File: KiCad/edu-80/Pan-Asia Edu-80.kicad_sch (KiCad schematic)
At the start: 24 parts, among them Q1 ED1402, Q2 ED1402, U1 Z80CPU, U11 CD4093, U12 4027, U13 4001

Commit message: Working on removing edu-80-rescue symbol library
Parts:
- C4: symbol edu-80-rescue:CP1_Small-Device -> Edu-80_Symbols:CP1
- D1: symbol edu-80-rescue:D_Small_ALT-Device -> Edu-80_Symbols:D_Small
- L1: symbol edu-80-rescue:LTRIM-Device -> Edu-80_Symbols:LTRIM
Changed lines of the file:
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@@
     )
   )
-  (symbol (lib_id "edu-80-rescue:LTRIM-Device") (at 111.76 26.67 90) (unit 1)
+  (symbol (lib_id "Edu-80_Symbols:LTRIM") (at 111.76 26.67 90) (unit 1)
     (in_bom yes) (on_board yes) (dnp no)
     (property "Reference" "L1" (at 111.76 20.574 90)
@@
     )
   )
-  (symbol (lib_id "edu-80-rescue:D_Small_ALT-Device") (at 80.01 74.93 270) (unit 1)
+  (symbol (lib_id "Edu-80_Symbols:D_Small") (at 80.01 74.93 270) (unit 1)
     (in_bom yes) (on_board yes) (dnp no)
     (property "Reference" "D1" (at 76.2 74.93 90)
@@
     )
   )
-  (symbol (lib_id "edu-80-rescue:CP1_Small-Device") (at 53.34 74.93 0) (unit 1)
+  (symbol (lib_id "Edu-80_Symbols:CP1") (at 53.34 74.93 0) (unit 1)
     (in_bom yes) (on_board yes) (dnp no)
     (property "Reference" "C4" (at 50.419 76.0984 0)
@@
       (effects (font (size 1.27 1.27)) (justify right))
     )
-    (property "Footprint" "" (at 54.3052 78.74 0)
-      (effects (font (size 1.27 1.27)) hide)
-    )
+    (property "Footprint" "" (at 53.34 74.93 0)
+      (effects (font (size 1.27 1.27)) hide)
+    )

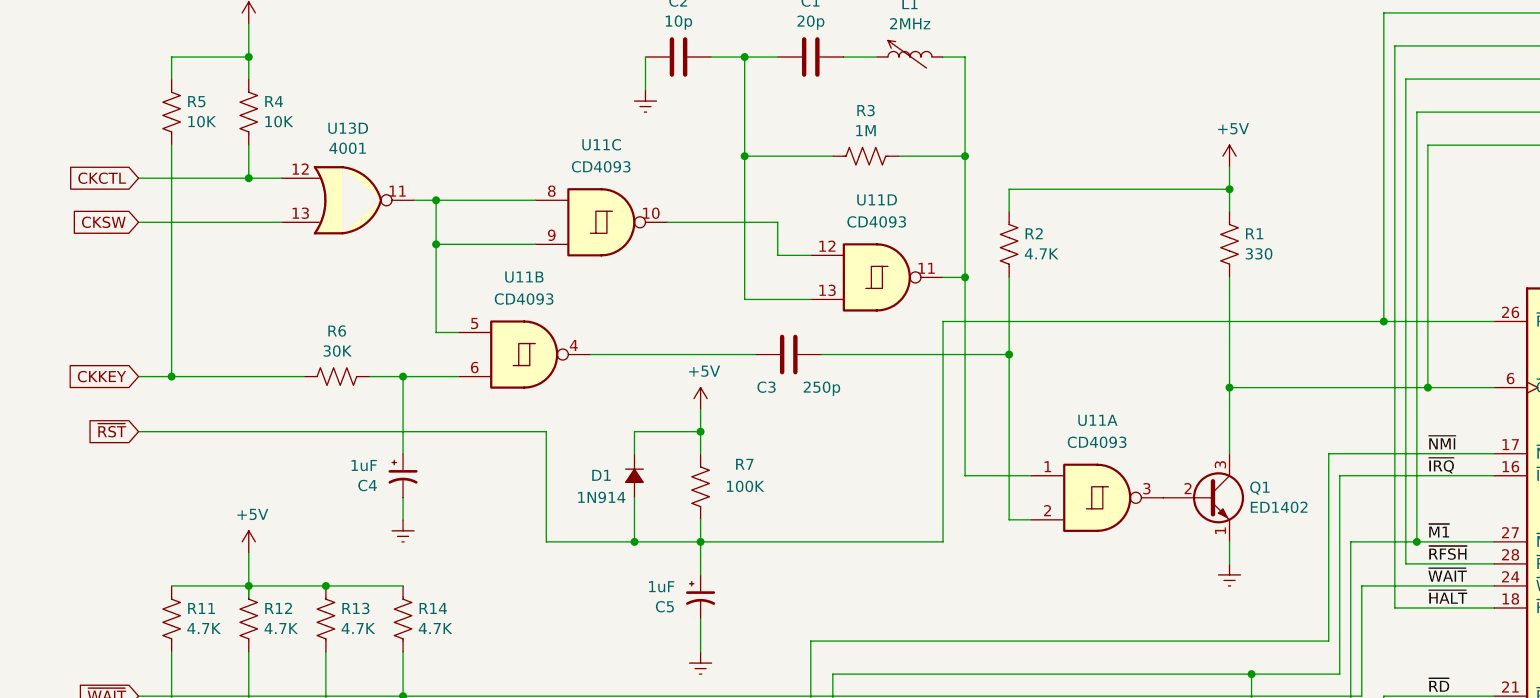
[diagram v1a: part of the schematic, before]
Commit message: Cleaning up the PAL-003 decoding, adding Modifications page.
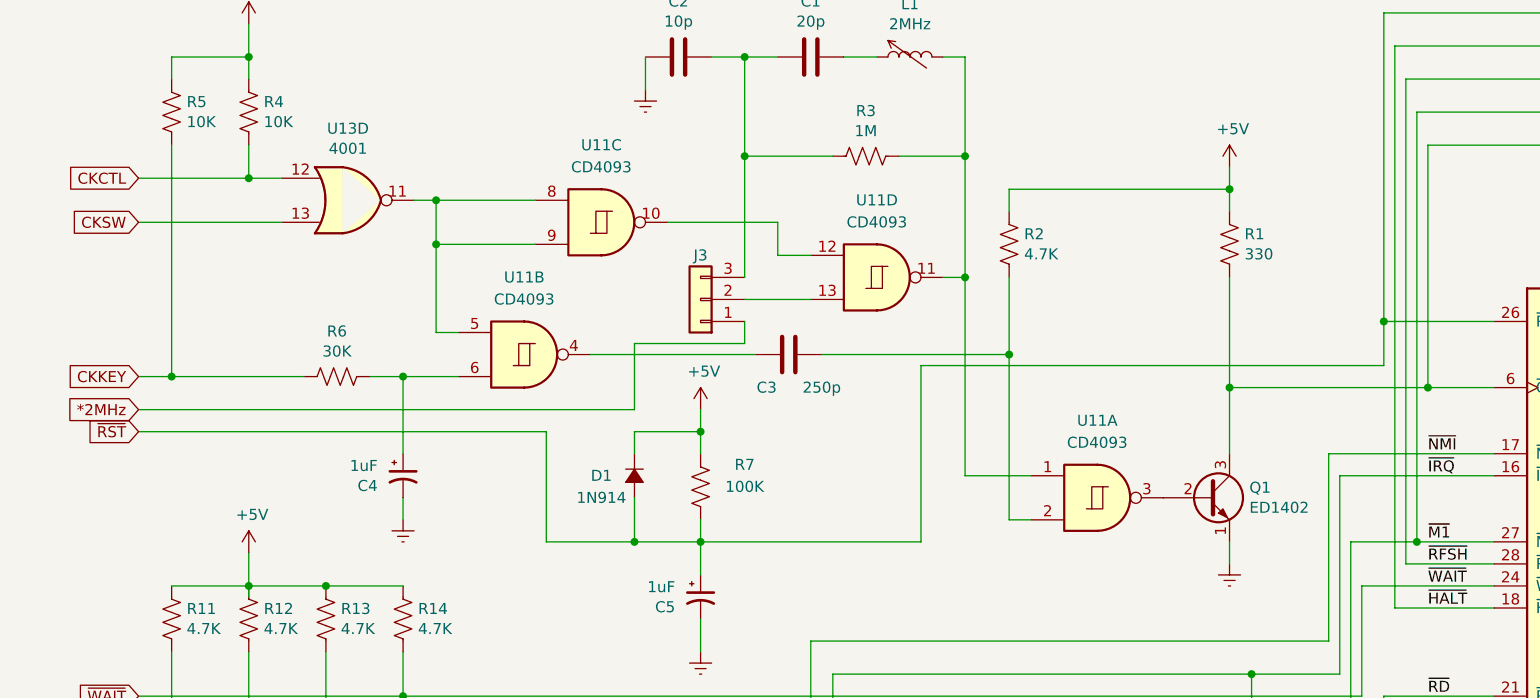
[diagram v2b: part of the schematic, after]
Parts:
- added J3: Conn_01x03, symbol Connector_Generic:Conn_01x03
- C5: symbol edu-80-rescue:CP1_Small-Device -> Edu-80_Symbols:CP1
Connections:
- net at C1.2, C2.1, R3.2: now also J3.3 (Pin_3); no longer U11.13
- new net: J3.2 (Pin_2), U11.13
- new net *2MHz: J3.1 (Pin_1)
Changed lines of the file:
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@@
   (title_block
     (title "Edu-80 Z80 Trainer")
-    (date "2023-02-06")
+    (date "2023-06-03")
     (rev "0.1")
     (company "Strangers")
+    (comment 1 "Author: James D. Tucker")
   )
   (junction (at 171.45 64.77) (diameter 0) (color 0 0 0 0)
@@
     (stroke (width 0) (type default))
   )
+  (wire (pts (xy 80.01 59.69) (xy 80.01 67.31))
+    (stroke (width 0) (type default))
+  )
   (wire (pts (xy 167.64 90.17) (xy 167.64 25.4))
     (stroke (width 0) (type default))
@@
     (stroke (width 0) (type default))
   )
-  (wire (pts (xy 87.63 82.55) (xy 115.57 82.55))
+  (wire (pts (xy 87.63 82.55) (xy 113.03 82.55))
     (stroke (width 0) (type default))
   )
@@
     (stroke (width 0) (type default))
   )
+  (wire (pts (xy 92.71 59.69) (xy 80.01 59.69))
+    (stroke (width 0) (type default))
+  )
   (wire (pts (xy 90.17 143.51) (xy 85.09 143.51))
     (stroke (width 0) (type default))
@@
     (stroke (width 0) (type default))
   )
-  (wire (pts (xy 92.71 38.1) (xy 92.71 54.61))
+  (wire (pts (xy 92.71 38.1) (xy 92.71 52.07))
     (stroke (width 0) (type default))
   )
@@
     (stroke (width 0) (type default))
   )
+  (wire (pts (xy 166.37 62.23) (xy 166.37 57.15))
+    (stroke (width 0) (type default))
+  )
   (wire (pts (xy 163.83 87.63) (xy 163.83 100.33))
     (stroke (width 0) (type default))
@@
     (stroke (width 0) (type default))
   )
-  (wire (pts (xy 115.57 57.15) (xy 166.37 57.15))
+  (wire (pts (xy 113.03 62.23) (xy 166.37 62.23))
     (stroke (width 0) (type default))
   )
@@
     (stroke (width 0) (type default))
   )
+  (wire (pts (xy 22.86 67.31) (xy 80.01 67.31))
+    (stroke (width 0) (type default))
+  )
   (wire (pts (xy 69.85 69.85) (xy 69.85 82.55))
     (stroke (width 0) (type default))
@@
     (stroke (width 0) (type default))
   )
+  (wire (pts (xy 92.71 57.15) (xy 92.71 59.69))
+    (stroke (width 0) (type default))
+  )
   (wire (pts (xy 168.91 153.67) (xy 254 153.67))
     (stroke (width 0) (type default))
@@
     (stroke (width 0) (type default))
   )
-  (wire (pts (xy 115.57 82.55) (xy 115.57 57.15))
+  (wire (pts (xy 113.03 82.55) (xy 113.03 62.23))
     (stroke (width 0) (type default))
   )
@@
     (effects (font (size 1.27 1.27)) (justify right))
     (property "Intersheetrefs" "${INTERSHEET_REFS}" (at 21.59 157.48 0)
+      (effects (font (size 1.27 1.27)) hide)
+    )
+  )
+  (global_label "*2MHz" (shape input) (at 22.86 67.31 180)
+    (effects (font (size 1.27 1.27)) (justify right))
+    (property "Intersheetrefs" "${INTERSHEET_REFS}" (at 22.86 67.31 0)
       (effects (font (size 1.27 1.27)) hide)
     )
@@
     )
   )
-  (symbol (lib_id "edu-80-rescue:CP1_Small-Device") (at 87.63 88.9 0) (unit 1)
+  (symbol (lib_id "Edu-80_Symbols:CP1") (at 87.63 88.9 0) (unit 1)
     (in_bom yes) (on_board yes) (dnp no)
     (property "Reference" "C5" (at 84.709 90.0684 0)
@@
       (effects (font (size 1.27 1.27)) (justify right))
     )
-    (property "Footprint" "" (at 88.5952 92.71 0)
+    (property "Footprint" "" (at 87.63 88.9 0)
       (effects (font (size 1.27 1.27)) hide)
     )
@@
         )
       )
+    )
+  )
+  (symbol (lib_id "Connector_Generic:Conn_01x03") (at 87.63 54.61 180) (unit 1)
+    (in_bom yes) (on_board yes) (dnp no)
+    (property "Reference" "J3" (at 87.63 49.53 0)
+      (effects (font (size 1.27 1.27)))
+    )
+    (property "Value" "Conn_01x03" (at 87.63 48.26 0)
+      (effects (font (size 1.27 1.27)) hide)
+    )
+    (property "Footprint" "" (at 87.63 54.61 0)
+      (effects (font (size 1.27 1.27)) hide)
+    )
+    (property "Datasheet" "~" (at 87.63 54.61 0)
+      (effects (font (size 1.27 1.27)) hide)
+    )
+    (pin "1")
+    (pin "2")
+    (pin "3")
+    (instances
+      (project "edu-80"
+        (path "/d19d6db6-a96a-43e3-aa50-c057821f7e22/00000000-0000-0000-0000-00006509b9c9"
+          (reference "J3") (unit 1)
+        )
+      )

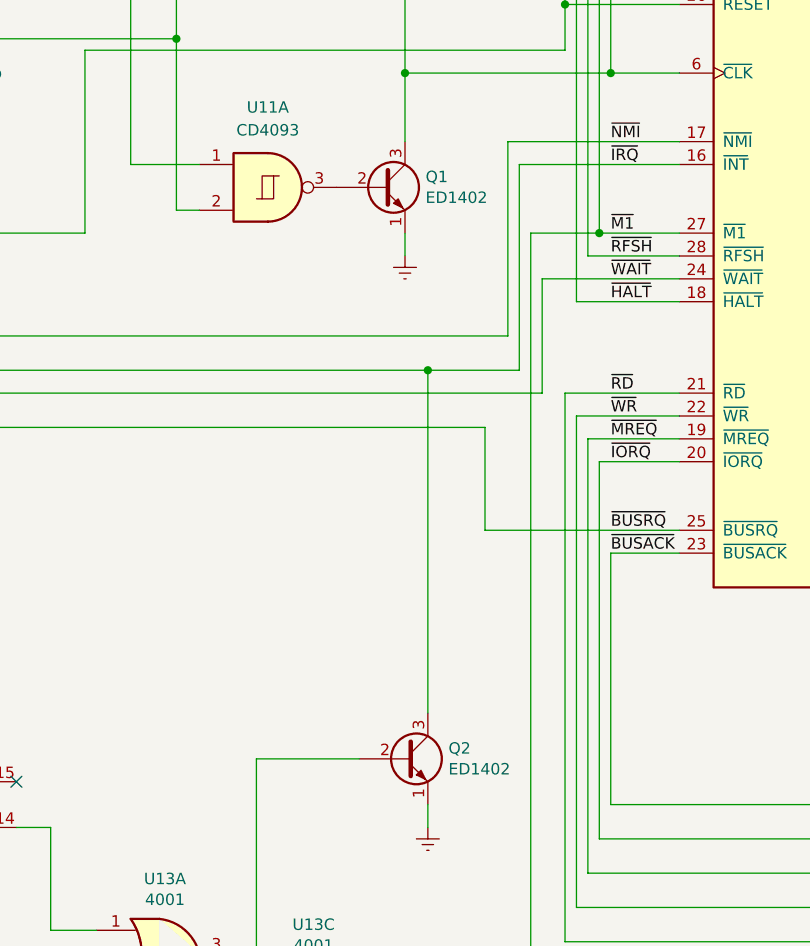
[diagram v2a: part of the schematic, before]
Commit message: Fixed ~IRQ vs. INT for PIO/CTC. Removed old (version 5) schematic files.
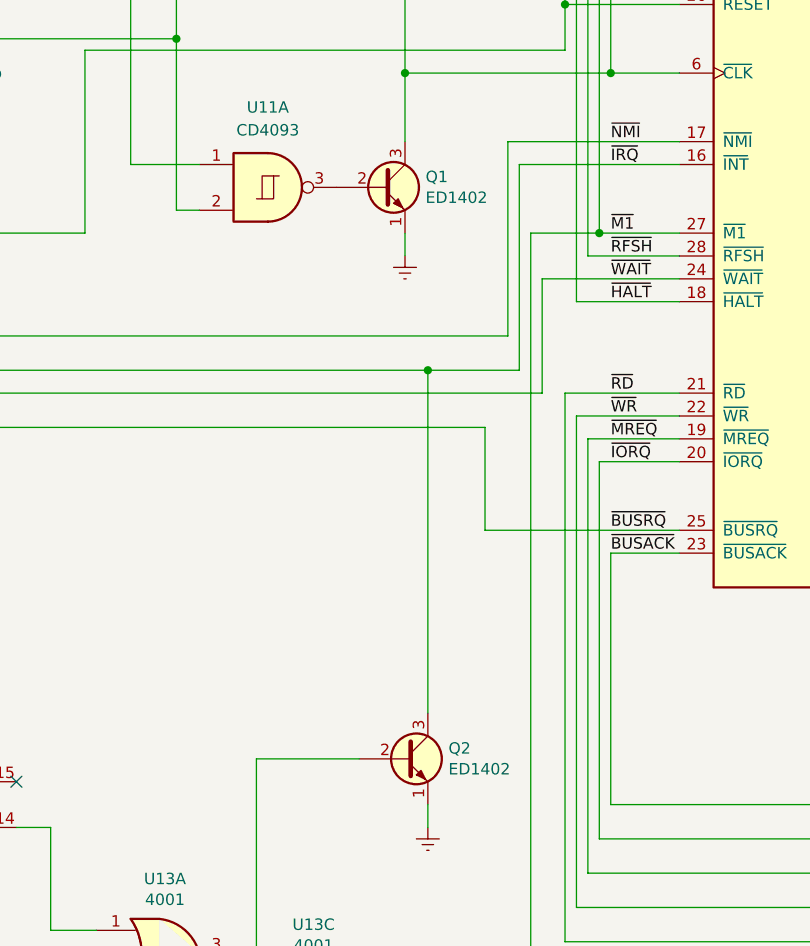
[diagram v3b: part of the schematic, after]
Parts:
- Q1, Q2: symbol Device:Q_NPN_EBC -> Edu-80_Symbols:Q_NPN_EBC
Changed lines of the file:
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@@
   (title_block
     (title "Edu-80 Z80 Trainer")
-    (date "2023-06-03")
+    (date "2023-06-05")
     (rev "0.1")
     (company "Strangers")
-    (comment 1 "Author: James D. Tucker")
+    (comment 4 "Author: James D. Tucker")
   )
   (junction (at 171.45 64.77) (diameter 0) (color 0 0 0 0)
@@
     )
   )
-  (symbol (lib_id "Device:Q_NPN_EBC") (at 146.05 77.47 0) (unit 1)
+  (symbol (lib_id "Edu-80_Symbols:Q_NPN_EBC") (at 146.05 77.47 0) (unit 1)
     (in_bom yes) (on_board yes) (dnp no)
     (property "Reference" "Q1" (at 150.876 76.3016 0)
@@
     )
   )
-  (symbol (lib_id "Device:Q_NPN_EBC") (at 148.59 140.97 0) (unit 1)
+  (symbol (lib_id "Edu-80_Symbols:Q_NPN_EBC") (at 148.59 140.97 0) (unit 1)
     (in_bom yes) (on_board yes) (dnp no)
     (property "Reference" "Q2" (at 153.416 139.8016 0)

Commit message: Fixed the last of the EDR warnings/errors, adding footprints
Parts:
- C4, C5: footprint (none) -> Capacitor_THT:CP_Radial_D5.0mm_P2.50mm
- D1: footprint (none) -> Diode_THT:D_A-405_P10.16mm_Horizontal
- L1: footprint (none) -> Inductor_THT:L_Radial_D10.0mm_P5.00mm_Fastron_07M
- Q1, Q2: footprint (none) -> Package_TO_SOT_THT:TO-92_Inline
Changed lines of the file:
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@@
       (effects (font (size 1.27 1.27)) hide)
     )
-    (property "Datasheet" "" (at 76.2 45.72 0)
+    (property "Datasheet" "https://assets.nexperia.com/documents/data-sheet/HEF4093B.pdf" (at 76.2 45.72 0)
       (effects (font (size 1.27 1.27)) hide)
     )
@@
       (effects (font (size 1.27 1.27)) hide)
     )
-    (property "Datasheet" "" (at 107.95 52.07 0)
+    (property "Datasheet" "https://assets.nexperia.com/documents/data-sheet/HEF4093B.pdf" (at 107.95 52.07 0)
       (effects (font (size 1.27 1.27)) hide)
     )
@@
       (effects (font (size 1.27 1.27)) hide)
     )
-    (property "Datasheet" "" (at 133.35 77.47 0)
+    (property "Datasheet" "https://assets.nexperia.com/documents/data-sheet/HEF4093B.pdf" (at 133.35 77.47 0)
       (effects (font (size 1.27 1.27)) hide)
     )
@@
       (effects (font (size 1.27 1.27)) hide)
     )
-    (property "Datasheet" "" (at 67.31 60.96 0)
+    (property "Datasheet" "https://assets.nexperia.com/documents/data-sheet/HEF4093B.pdf" (at 67.31 60.96 0)
       (effects (font (size 1.27 1.27)) hide)
     )
@@
       (effects (font (size 1.27 1.27)))
     )
-    (property "Footprint" "" (at 111.76 26.67 0)
+    (property "Footprint" "Inductor_THT:L_Radial_D10.0mm_P5.00mm_Fastron_07M" (at 111.76 26.67 0)
       (effects (font (size 1.27 1.27)) hide)
     )
@@
       (effects (font (size 1.27 1.27)) (justify right))
     )
-    (property "Footprint" "" (at 87.63 88.9 0)
+    (property "Footprint" "Capacitor_THT:CP_Radial_D5.0mm_P2.50mm" (at 87.63 88.9 0)
       (effects (font (size 1.27 1.27)) hide)
     )
@@
       (effects (font (size 1.27 1.27)))
     )
-    (property "Footprint" "" (at 80.01 74.93 90)
+    (property "Footprint" "Diode_THT:D_A-405_P10.16mm_Horizontal" (at 80.01 74.93 90)
       (effects (font (size 1.27 1.27)) hide)
     )
@@
       (effects (font (size 1.27 1.27)) (justify right))
     )
-    (property "Footprint" "" (at 53.34 74.93 0)
+    (property "Footprint" "Capacitor_THT:CP_Radial_D5.0mm_P2.50mm" (at 53.34 74.93 0)
       (effects (font (size 1.27 1.27)) hide)
     )
@@
       (effects (font (size 1.27 1.27)) (justify left))
     )
-    (property "Footprint" "" (at 151.13 74.93 0)
+    (property "Footprint" "Package_TO_SOT_THT:TO-92_Inline" (at 151.13 74.93 0)
       (effects (font (size 1.27 1.27)) hide)
     )
@@
       (effects (font (size 1.27 1.27)) (justify left))
     )
-    (property "Footprint" "" (at 153.67 138.43 0)
-      (effects (font (size 1.27 1.27)) hide)
-    )
+    (property "Footprint" "Package_TO_SOT_THT:TO-92_Inline" (at 153.67 138.43 0)
+      (effects (font (size 1.27 1.27)) hide)
+    )
